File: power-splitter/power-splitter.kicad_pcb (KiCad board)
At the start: 2 copper layers, 52.6 x 49.1 mm, 17 parts, among them J1 Barrel_Jack, J2 USB_B_Micro, J3 Conn_01x02_Pin, J4 Conn_01x02_Pin, J5 Conn_02x02_Counter_Clockwise, SW1 SW_SP3T, U1 LM2594M-3.3

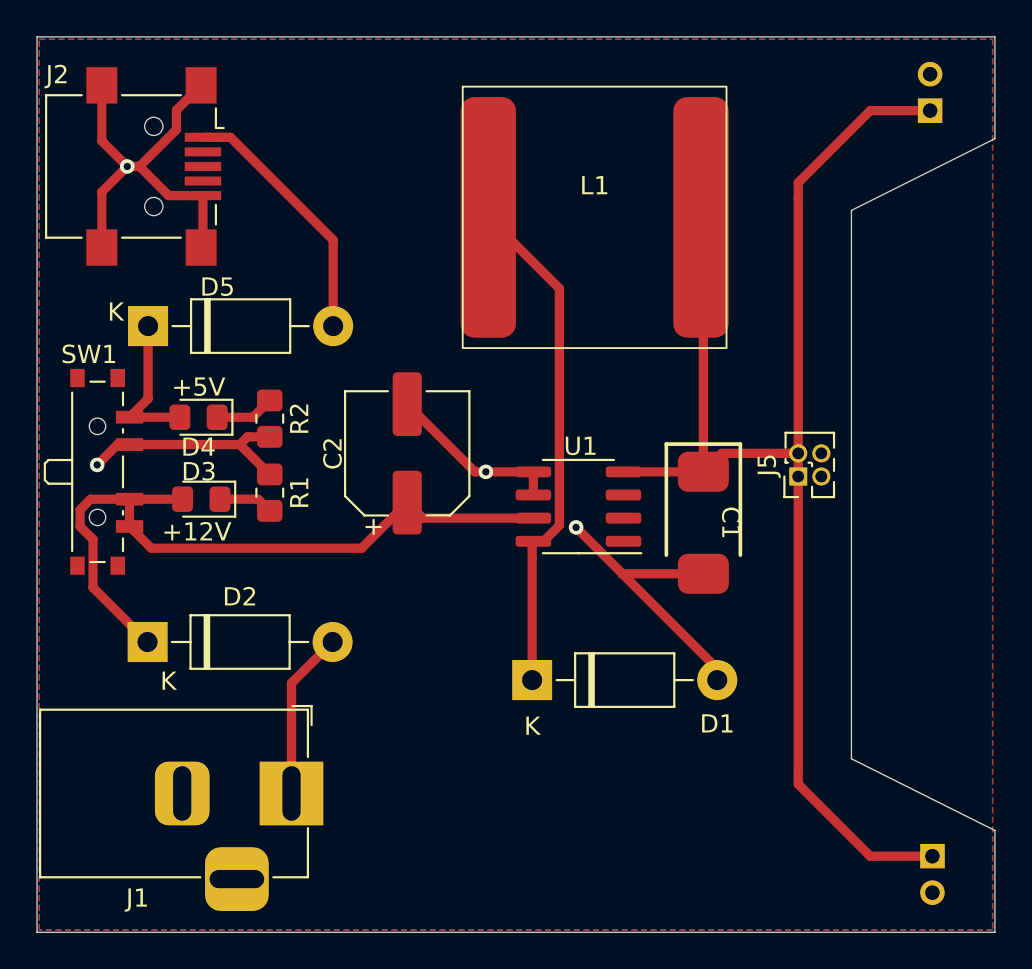
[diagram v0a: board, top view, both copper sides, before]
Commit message: Updated layout
+ Adjusted ground pours
+ Adjusted power pours
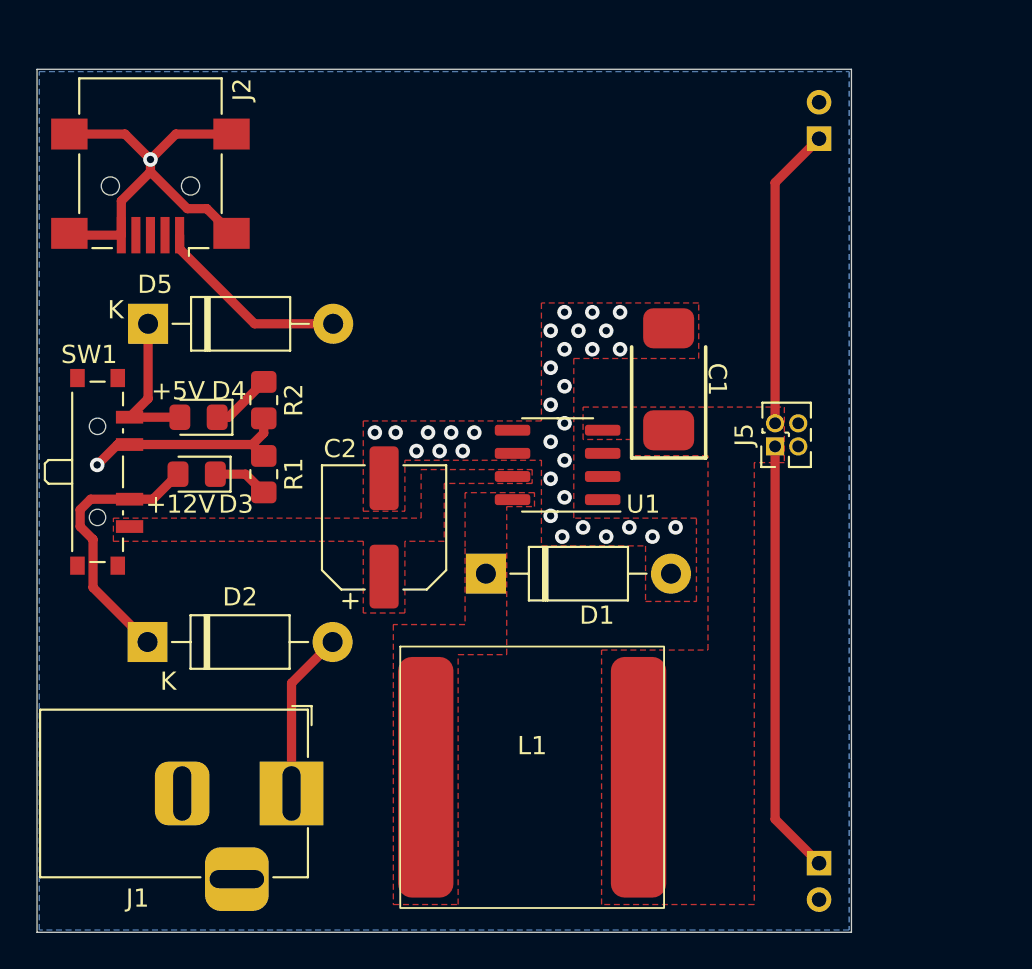
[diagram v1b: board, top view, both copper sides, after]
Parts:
- moved L1 30.9 mm to (59.7, 98.6)
- moved C1 8.10 mm to (67.2, 76.7), turned to 90 degrees
- moved D1 6.37 mm to (57.1, 87.4)
- moved J3 6.29 mm to (75.4, 63.5)
- moved J4 6.23 mm to (75.4, 103.3)
- moved C2 4.26 mm to (51.6, 84.8)
- moved U1 2.56 mm to (61.1, 81.4)
- moved J5 2.08 mm to (73.0, 80.4)
- moved D3 1.39 mm to (41.3, 81.9)
- moved J2 1.09 mm to (38.7, 66.1), turned to 180 degrees
- moved R2 1.07 mm to (45.0, 77.9)
- moved R1 1.07 mm to (45.0, 81.9)
- moved D5 0.13 mm to (38.6, 73.7)
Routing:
- net +3V3: track 74.9 -> 40.5 mm
- net Net-(D1-K): track 28.0 -> 0.00 mm
- net GND: track 62.4 -> 35.2 mm, vias 4 -> 34
- net +12V: track 40.2 -> 15.0 mm
- net Net-(D5-A): track 14.2 -> 10.9 mm
- added copper zone on F.Cu, net +12V
- added copper zone on F.Cu, net +3V3
- added copper zone on F.Cu, net GND
- added copper zone on F.Cu, net Net-(D1-K)
- removed copper zone on F.Cu, net (none)
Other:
- board size 52.6 x 49.1 mm -> 44.7 x 47.4 mm

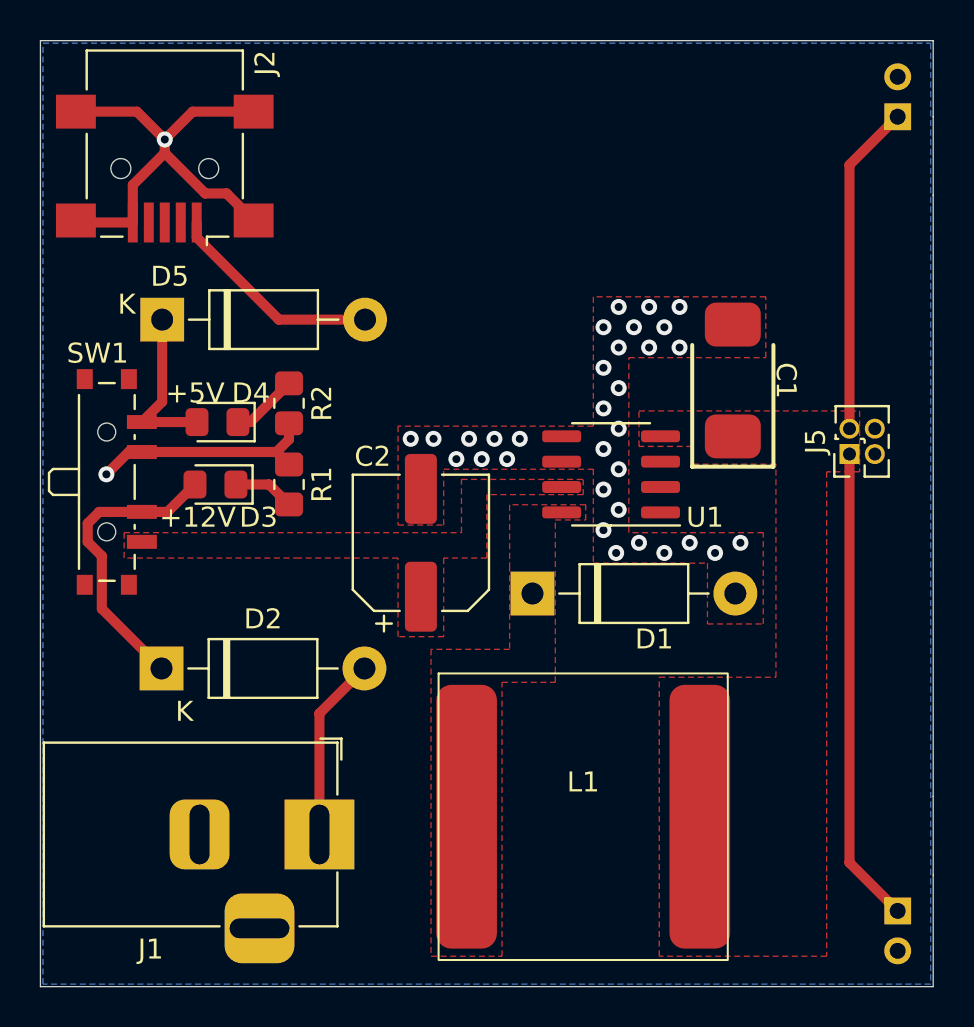
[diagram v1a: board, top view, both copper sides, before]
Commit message: Updated schem/layout
+ Adjusted pours to filet edges
+ Added text for +3V3 outputs
+ Adjusted board edges to be less weird
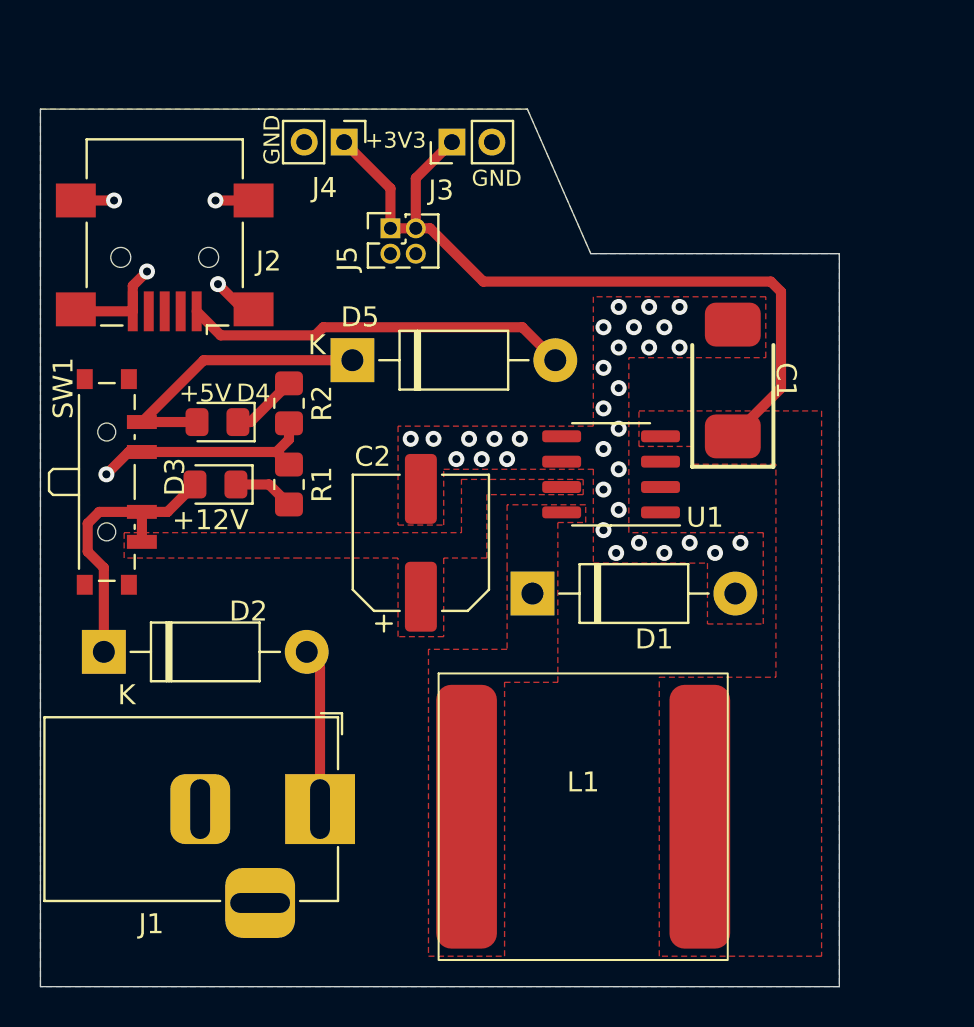
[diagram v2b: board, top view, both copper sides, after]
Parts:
- J3, J4: moved to F.Cu
- moved J4 47.4 mm to (47.7, 64.8), turned to -90 degrees
- moved J5 25.6 mm to (50.0, 69.1), turned to 0 degrees
- moved J3 22.4 mm to (53.1, 64.8), turned to 90 degrees
- moved D5 9.74 mm to (48.1, 75.7)
- moved J2 4.45 mm to (38.7, 70.5)
- moved D2 3.01 mm to (35.7, 90.3)
- moved J1 1.27 mm to (46.5, 98.2)
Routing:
- net GND: track 35.2 -> 22.9 mm, vias 34 -> 37
- net Net-(D5-A): track 10.9 -> 19.3 mm
- net +5V: track 8.31 -> 14.6 mm
- net Net-(D2-A): track 9.25 -> 8.20 mm
- net +3V3: track 40.5 -> 39.5 mm
- net +12V: track 15.0 -> 14.4 mm
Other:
- board size 44.7 x 47.4 mm -> 40 x 43.9 mm
- board text added: "+3V3"
- board text added: "GND"

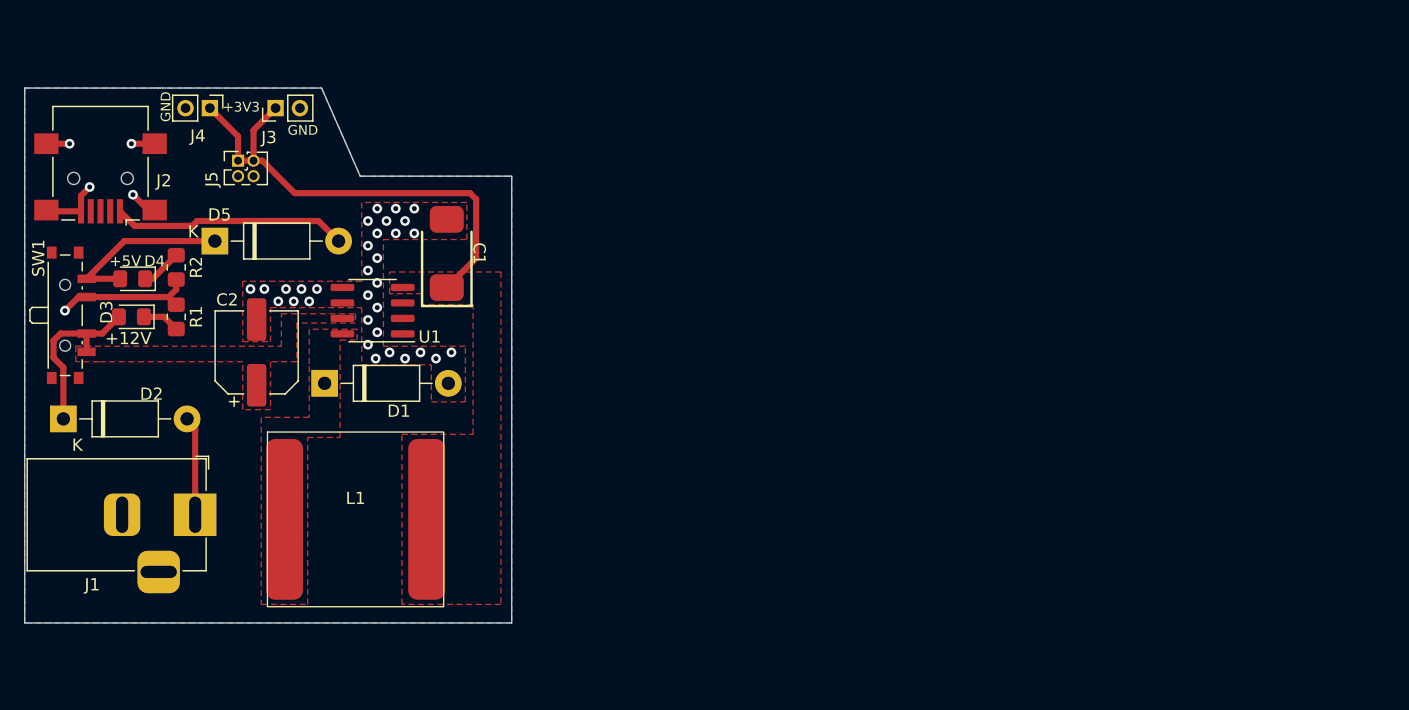
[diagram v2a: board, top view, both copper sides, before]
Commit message: Updated to Rev B
+ Adjusted layout to be more compact and to fit on 51mm wide breadboards
+ Added 3D STEP files for the barrel jack, USB-Micro B receptacle
+ Added PDFs for the schematic and top/bottom layer of the PCB
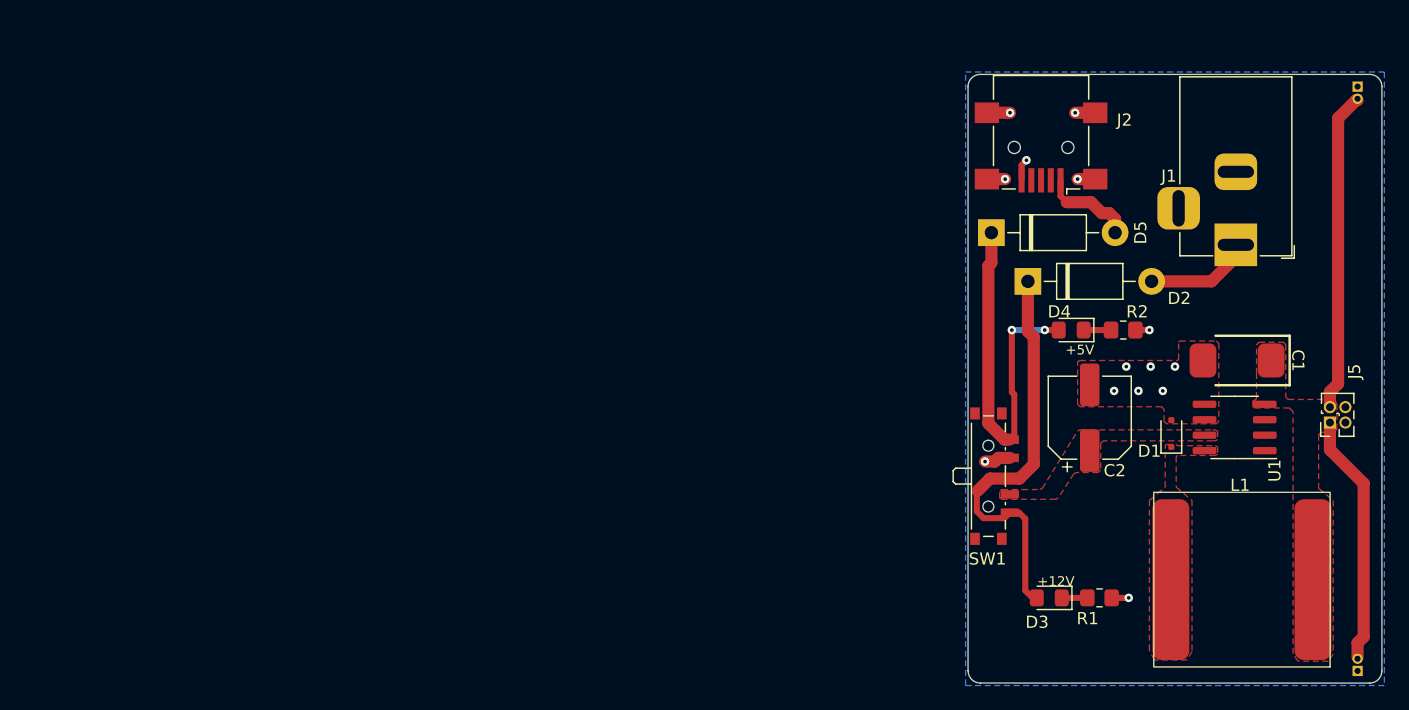
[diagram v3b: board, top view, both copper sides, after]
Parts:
- D1: value 1N5817 -> SC-90; footprint Diode_THT:D_DO-41_SOD81_P10.16mm_Horizontal -> Diode_SMD:D_SOD-323F
- J3, J4: value Conn_01x02_Pin -> Conn_01x02; footprint Connector_PinHeader_2.00mm:PinHeader_1x02_P2.00mm_Vertical -> Connector_PinHeader_1.00mm:PinHeader_1x02_P1.00mm_Vertical; moved to B.Cu
- moved J3 100.2 mm to (142.0, 111.0), turned to 0 degrees
- moved J4 94.3 mm to (142.0, 63.0), turned to 180 degrees
- moved J5 92.2 mm to (139.7, 90.6), turned to 90 degrees
- moved J1 88.3 mm to (132.0, 76.0), turned to -90 degrees
- moved D2 80.0 mm to (114.9, 79.0)
- moved R1 79.3 mm to (120.8, 105.0), turned to 0 degrees
- moved D3 78.9 mm to (116.7, 105.0)
- moved R2 78.0 mm to (122.8, 83.0), turned to 0 degrees
- moved J2 77.3 mm to (116.0, 68.0)
- moved D4 77.2 mm to (118.5, 83.0)
- moved SW1 77.0 mm to (112.0, 95.0)
- moved L1 73.0 mm to (132.5, 103.5), turned to 180 degrees
- moved U1 71.5 mm to (131.9, 91.0)
- moved D1 69.7 mm to (126.7, 91.5), turned to 90 degrees
- moved C2 68.6 mm to (120.0, 90.2)
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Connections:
- J3 pad 1: +3V3 -> GND
- J3 pad 2: GND -> +3V3
- J4 pad 1: +3V3 -> GND
- J4 pad 2: GND -> +3V3
- L1 pad 1: Net-(D1-K) -> +3V3
- L1 pad 2: +3V3 -> Net-(D1-K)
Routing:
- net +12V: track 14.4 -> 34.2 mm
- net +5V: track 14.6 -> 31.2 mm, vias 0 -> 2
- net Net-(D5-A): track 19.3 -> 7.68 mm
- net GND: track 22.9 -> 13.0 mm, vias 37 -> 14
- net +3V3: track 39.5 -> 46.8 mm
- net Net-(D4-K): track 3.36 -> 2.25 mm
- net Net-(D3-K): track 3.07 -> 2.10 mm
- net Net-(D2-A): track 8.20 -> 8.75 mm
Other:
- board size 40 x 43.9 mm -> 34 x 50 mm
- board text added: "+12V"
- board text added: "+5V"
- board text removed: "+3V3"
- board text removed: "GND"
